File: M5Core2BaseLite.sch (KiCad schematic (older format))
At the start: 25 parts, among them CN1 CON_GROVEH, CN2 CON_GROVEH, CN3 CON_GROVEH, CN4 CON_GROVEH, CN5 CON_GROVEV, CN6 MBUS_bottom, CN8 CON_GROVEH, CN9 CON_GROVEH, J1 Conn_01x02_Female, J2 Conn_01x02_Female, J3 Conn_01x08_Female, U1 LED_SK6812side, U10 LED_SK6812side, U2 LED_SK6812side, U3 LED_SK6812side, U4 LED_SK6812side, U5 LED_SK6812side, U6 LED_SK6812side, U7 LED_SK6812side, U8 LED_SK6812side, U9 LED_SK6812side

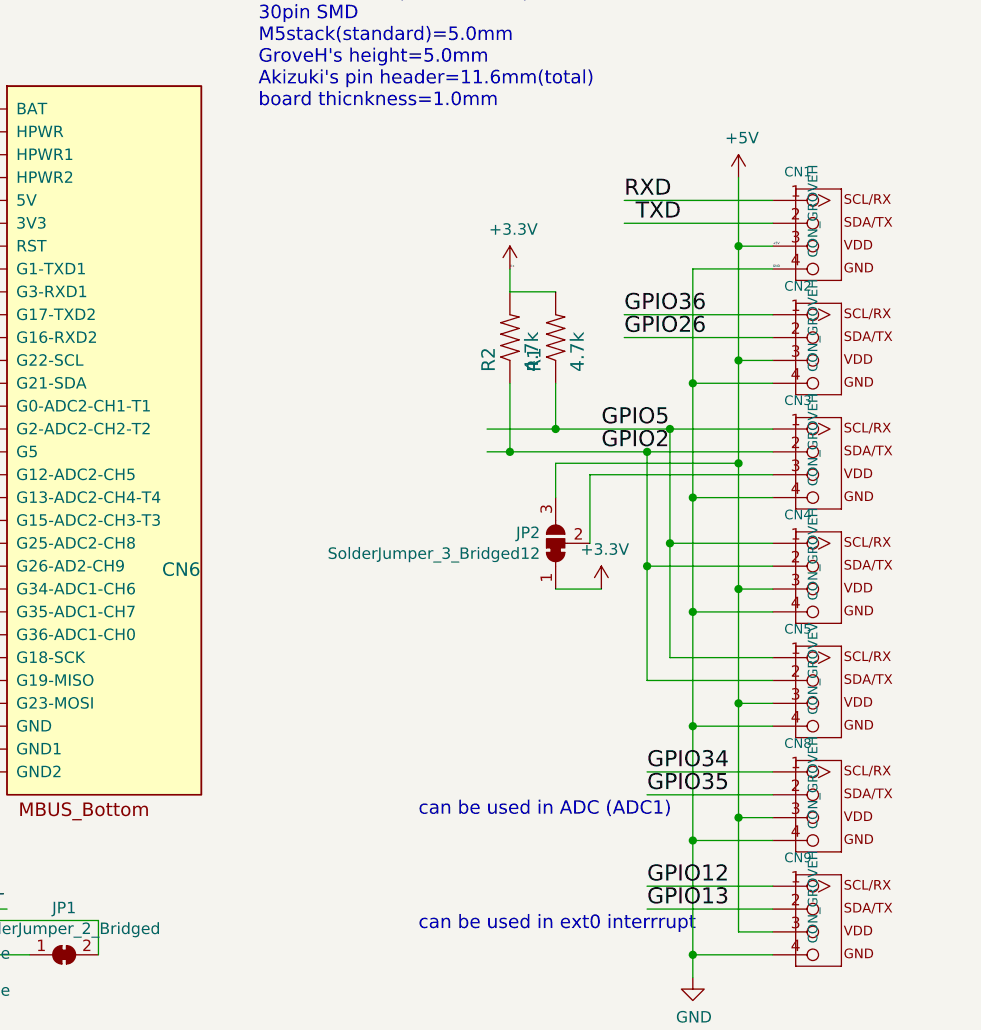
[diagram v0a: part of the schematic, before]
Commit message: 基板データをv1.0a（PortA'をデフォルト5V）に変更
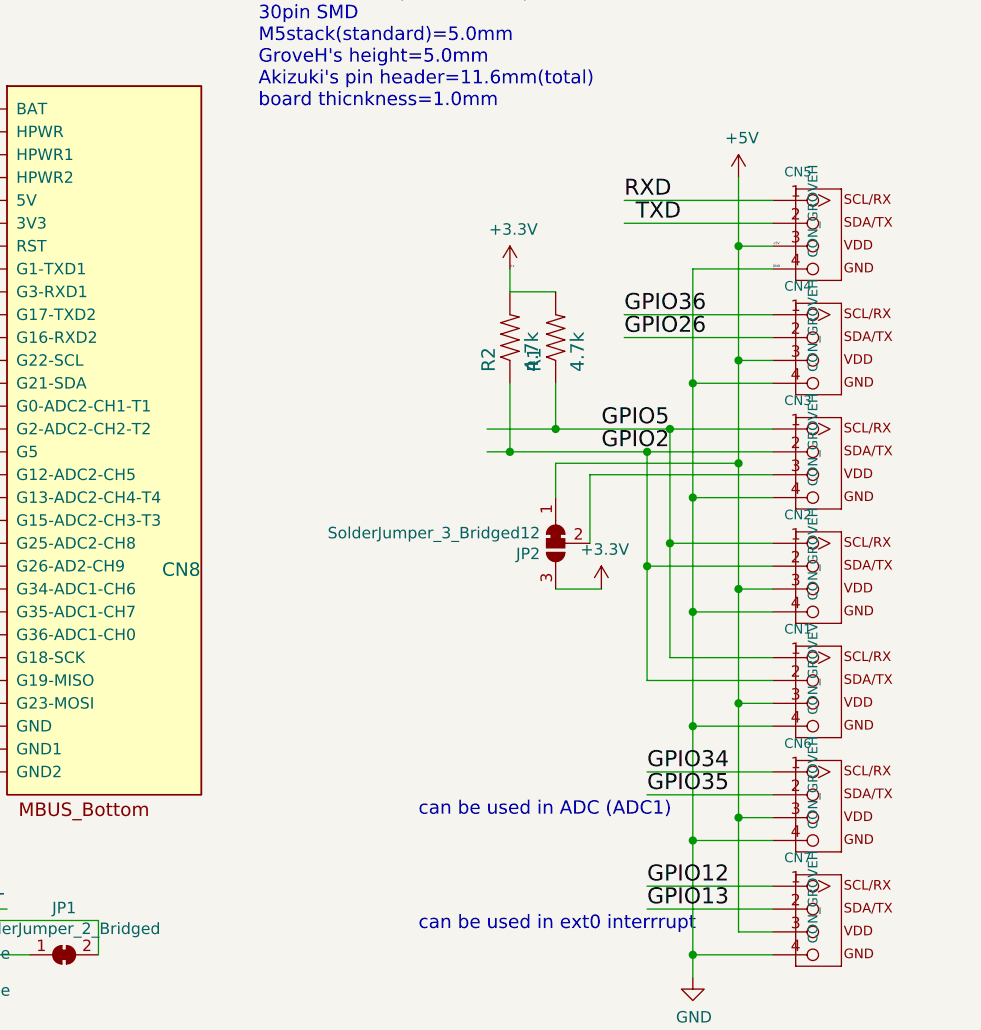
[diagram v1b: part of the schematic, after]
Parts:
- renumbered CN5 to CN1, CN4 to CN2, CN2 to CN4, CN1 to CN5, CN8 to CN6, CN9 to CN7, CN6 to CN8
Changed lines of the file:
@@
 GPIO12
 $Comp
-L M5Core2BaseLite-rescue:CON_GROVEH-M5GObase_sub-eagle-import-M5GOBaseLite-rescue CN1
+L M5Core2BaseLite-rescue:CON_GROVEH-M5GObase_sub-eagle-import-M5GOBaseLite-rescue CN5
 U 1 1 496D2C97
 P 8250 2900
-F 0 "CN1" H 8200 3100 42  0000 L BNN
+F 0 "CN5" H 8200 3100 42  0000 L BNN
 F 1 "CON_GROVEH" V 8350 2750 42  0000 L BNN
 F 2 "M5GObase_sub:CON_GROVE_H" H 8250 2900 50  0001 C CNN
@@
 $EndComp
 $Comp
-L M5Core2BaseLite-rescue:CON_GROVEH-M5GObase_sub-eagle-import-M5GOBaseLite-rescue CN2
+L M5Core2BaseLite-rescue:CON_GROVEH-M5GObase_sub-eagle-import-M5GOBaseLite-rescue CN4
 U 1 1 3E9C7CC7
 P 8250 3400
-F 0 "CN2" H 8200 3600 42  0000 L BNN
+F 0 "CN4" H 8200 3600 42  0000 L BNN
 F 1 "CON_GROVEH" V 8350 3250 42  0000 L BNN
 F 2 "M5GObase_sub:CON_GROVE_H" H 8250 3400 50  0001 C CNN
@@
 $EndComp
 $Comp
-L M5Core2BaseLite-rescue:CON_GROVEH-M5GObase_sub-eagle-import-M5GOBaseLite-rescue CN4
+L M5Core2BaseLite-rescue:CON_GROVEH-M5GObase_sub-eagle-import-M5GOBaseLite-rescue CN2
 U 1 1 61EA98FF
 P 8250 4400
-F 0 "CN4" H 8200 4600 42  0000 L BNN
+F 0 "CN2" H 8200 4600 42  0000 L BNN
 F 1 "CON_GROVEH" V 8350 4250 42  0000 L BNN
 F 2 "M5GObase_sub:CON_GROVE_H" H 8250 4400 50  0001 C CNN
@@
 $EndComp
 $Comp
-L M5Core2BaseLite-rescue:CON_GROVEV-M5GObase_sub-eagle-import-M5GOBaseLite-rescue CN5
+L M5Core2BaseLite-rescue:CON_GROVEV-M5GObase_sub-eagle-import-M5GOBaseLite-rescue CN1
 U 1 1 4DB63874
 P 8250 4900
-F 0 "CN5" H 8200 5100 42  0000 L BNN
+F 0 "CN1" H 8200 5100 42  0000 L BNN
 F 1 "CON_GROVEV" V 8350 4750 42  0000 L BNN
 F 2 "M5GObase_sub:CON_GROVE_V" H 8250 4900 50  0001 C CNN
@@
 $EndComp
 $Comp
-L M5Core2BaseLite-rescue:CON_GROVEH-M5GObase_sub-eagle-import-M5GOBaseLite-rescue CN8
+L M5Core2BaseLite-rescue:CON_GROVEH-M5GObase_sub-eagle-import-M5GOBaseLite-rescue CN6
 U 1 1 99C0620C
 P 8250 5400
-F 0 "CN8" H 8200 5600 42  0000 L BNN
+F 0 "CN6" H 8200 5600 42  0000 L BNN
 F 1 "CON_GROVEH" V 8350 5250 42  0000 L BNN
 F 2 "M5GObase_sub:CON_GROVE_H" H 8250 5400 50  0001 C CNN
@@
 $EndComp
 $Comp
-L M5Core2BaseLite-rescue:CON_GROVEH-M5GObase_sub-eagle-import-M5GOBaseLite-rescue CN9
+L M5Core2BaseLite-rescue:CON_GROVEH-M5GObase_sub-eagle-import-M5GOBaseLite-rescue CN7
 U 1 1 86A80BA3
 P 8250 5900
-F 0 "CN9" H 8200 6100 42  0000 L BNN
+F 0 "CN7" H 8200 6100 42  0000 L BNN
 F 1 "CON_GROVEH" V 8350 5750 42  0000 L BNN
 F 2 "M5GObase_sub:CON_GROVE_H" H 8250 5900 50  0001 C CNN
@@
 	3600 1550 3600 1650
 $Comp
-L akita:MBUS_bottom CN6
+L akita:MBUS_bottom CN8
 U 1 1 5E3A0B90
 P 5250 3700
-F 0 "CN6" H 5478 2985 59  0000 L CNN
+F 0 "CN8" H 5478 2985 59  0000 L CNN
 F 1 "MBUS_bottom" H 5250 3700 50  0001 C CNN
 F 2 "Connector_PinSocket_2.54mm:PinSocket_2x15_P2.54mm_Vertical_SMD" H 5250 3700 50  0001 C CNN
@@
 F 3 "~" H 7200 4300 50  0001 C CNN
 	1    7200 4300
-	0    -1   -1   0
-$EndComp
-Wire Wire Line
+	0    -1   1    0
+$EndComp
+Wire Wire Line
